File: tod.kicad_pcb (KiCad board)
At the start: 2 copper layers, 72 x 57 mm, 68 parts, among them J1 Conn_01x04, J2 Conn_01x03, J3 Conn_01x04, J4 Conn_01x03, Q1 BC856B, Q2 BC817, Q3 BC856B, Q4 BC817, Q5 BC856, Q6 BC817, Q7 BC856, Q8 BC817, U1 PC817, U2 PC817, U3 PC817, U4 PC817

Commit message: Use 2k resistors instead of 3k9.
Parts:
- R13, R18, R3, R8: value 3k9 -> 2k
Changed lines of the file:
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@@
     (descr "Resistor SMD 0805 (2012 Metric), square (rectangular) end terminal, IPC_7351 nominal with elongated pad for handsoldering. (Body size source: IPC-SM-782 page 72, https://www.pcb-3d.com/wordpress/wp-content/uploads/ipc-sm-782a_amendment_1_and_2.pdf), generated with kicad-footprint-generator")
     (tags "resistor handsolder")
-    (property "LCSC" "C17614")
+    (property "LCSC" "C17604")
     (property "Sheetfile" "tod.kicad_sch")
     (property "Sheetname" "")
@@
       (effects (font (size 1 1) (thickness 0.15)) (justify mirror))
     )
-    (fp_text value "3k9" (at 0 -1.65 90) (layer "B.Fab")
+    (fp_text value "2k" (at 0 -1.65 90) (layer "B.Fab")
       (effects (font (size 1 1) (thickness 0.15)) (justify mirror))
     )
@@
     (descr "SOD-323")
     (tags "SOD-323")
+    (property "JLCPCB_IGNORE" "-")
     (property "LCSC" "C191023")
     (property "Sheetfile" "tod.kicad_sch")
@@
     (descr "SOD-323")
     (tags "SOD-323")
+    (property "JLCPCB_IGNORE" "-")
     (property "LCSC" "C191023")
     (property "Sheetfile" "tod.kicad_sch")
@@
     (descr "Resistor SMD 0805 (2012 Metric), square (rectangular) end terminal, IPC_7351 nominal with elongated pad for handsoldering. (Body size source: IPC-SM-782 page 72, https://www.pcb-3d.com/wordpress/wp-content/uploads/ipc-sm-782a_amendment_1_and_2.pdf), generated with kicad-footprint-generator")
     (tags "resistor handsolder")
-    (property "LCSC" "C17614")
+    (property "LCSC" "C17604")
     (property "Sheetfile" "tod.kicad_sch")
     (property "Sheetname" "")
@@
       (effects (font (size 1 1) (thickness 0.15)) (justify mirror))
     )
-    (fp_text value "3k9" (at 0 -1.65 90) (layer "B.Fab")
+    (fp_text value "2k" (at 0 -1.65 90) (layer "B.Fab")
       (effects (font (size 1 1) (thickness 0.15)) (justify mirror))
     )
@@
     (descr "SOT, 3 Pin (https://www.jedec.org/system/files/docs/to-236h.pdf variant AB), generated with kicad-footprint-generator ipc_gullwing_generator.py")
     (tags "SOT TO_SOT_SMD")
-    (property "LCSC" "C2926215")
+    (property "LCSC" "C2149")
     (property "Sheetfile" "tod.kicad_sch")
     (property "Sheetname" "")
@@
     (descr "SOT, 3 Pin (https://www.jedec.org/system/files/docs/to-236h.pdf variant AB), generated with kicad-footprint-generator ipc_gullwing_generator.py")
     (tags "SOT TO_SOT_SMD")
-    (property "LCSC" "C2926215")
+    (property "LCSC" "C2149")
     (property "Sheetfile" "tod.kicad_sch")
     (property "Sheetname" "")
@@
     (descr "SOT, 3 Pin (https://www.jedec.org/system/files/docs/to-236h.pdf variant AB), generated with kicad-footprint-generator ipc_gullwing_generator.py")
     (tags "SOT TO_SOT_SMD")
-    (property "LCSC" "C2926215")
+    (property "LCSC" "C2149")
     (property "Sheetfile" "tod.kicad_sch")
     (property "Sheetname" "")
@@
     (descr "Resistor SMD 0805 (2012 Metric), square (rectangular) end terminal, IPC_7351 nominal with elongated pad for handsoldering. (Body size source: IPC-SM-782 page 72, https://www.pcb-3d.com/wordpress/wp-content/uploads/ipc-sm-782a_amendment_1_and_2.pdf), generated with kicad-footprint-generator")
     (tags "resistor handsolder")
-    (property "LCSC" "C17614")
+    (property "LCSC" "C17604")
     (property "Sheetfile" "tod.kicad_sch")
     (property "Sheetname" "")
@@
       (effects (font (size 1 1) (thickness 0.15)) (justify mirror))
     )
-    (fp_text value "3k9" (at 0 -1.65 90) (layer "B.Fab")
+    (fp_text value "2k" (at 0 -1.65 90) (layer "B.Fab")
       (effects (font (size 1 1) (thickness 0.15)) (justify mirror))
     )
@@
     (descr "Resistor SMD 0805 (2012 Metric), square (rectangular) end terminal, IPC_7351 nominal with elongated pad for handsoldering. (Body size source: IPC-SM-782 page 72, https://www.pcb-3d.com/wordpress/wp-content/uploads/ipc-sm-782a_amendment_1_and_2.pdf), generated with kicad-footprint-generator")
     (tags "resistor handsolder")
-    (property "LCSC" "C17614")
+    (property "LCSC" "C17604")
     (property "Sheetfile" "tod.kicad_sch")
     (property "Sheetname" "")
@@
       (effects (font (size 1 1) (thickness 0.15)) (justify mirror))
     )
-    (fp_text value "3k9" (at 0 -1.65 90) (layer "B.Fab")
+    (fp_text value "2k" (at 0 -1.65 90) (layer "B.Fab")
       (effects (font (size 1 1) (thickness 0.15)) (justify mirror))
     )
@@
     (descr "SOD-323")
     (tags "SOD-323")
+    (property "JLCPCB_IGNORE" "-")
     (property "LCSC" "C191023")
     (property "Sheetfile" "tod.kicad_sch")
@@
     (descr "SOT, 3 Pin (https://www.jedec.org/system/files/docs/to-236h.pdf variant AB), generated with kicad-footprint-generator ipc_gullwing_generator.py")
     (tags "SOT TO_SOT_SMD")
-    (property "LCSC" "C2926215")
+    (property "LCSC" "C2149")
     (property "Sheetfile" "tod.kicad_sch")
     (property "Sheetname" "")
@@
     (descr "SOD-323")
     (tags "SOD-323")
+    (property "JLCPCB_IGNORE" "-")
     (property "LCSC" "C191023")
     (property "Sheetfile" "tod.kicad_sch")

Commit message: Revert "Use 2k resistors instead of 3k9."
This reverts commit e4b48c20f046feec0504172c1823d5e465362b53.
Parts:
- R13, R18, R3, R8: value 2k -> 3k9
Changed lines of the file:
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@@
     (descr "Resistor SMD 0805 (2012 Metric), square (rectangular) end terminal, IPC_7351 nominal with elongated pad for handsoldering. (Body size source: IPC-SM-782 page 72, https://www.pcb-3d.com/wordpress/wp-content/uploads/ipc-sm-782a_amendment_1_and_2.pdf), generated with kicad-footprint-generator")
     (tags "resistor handsolder")
-    (property "LCSC" "C17604")
+    (property "LCSC" "C17614")
     (property "Sheetfile" "tod.kicad_sch")
     (property "Sheetname" "")
@@
       (effects (font (size 1 1) (thickness 0.15)) (justify mirror))
     )
-    (fp_text value "2k" (at 0 -1.65 90) (layer "B.Fab")
+    (fp_text value "3k9" (at 0 -1.65 90) (layer "B.Fab")
       (effects (font (size 1 1) (thickness 0.15)) (justify mirror))
     )
@@
     (descr "SOD-323")
     (tags "SOD-323")
-    (property "JLCPCB_IGNORE" "-")
     (property "LCSC" "C191023")
     (property "Sheetfile" "tod.kicad_sch")
@@
     (descr "SOD-323")
     (tags "SOD-323")
-    (property "JLCPCB_IGNORE" "-")
     (property "LCSC" "C191023")
     (property "Sheetfile" "tod.kicad_sch")
@@
     (descr "Resistor SMD 0805 (2012 Metric), square (rectangular) end terminal, IPC_7351 nominal with elongated pad for handsoldering. (Body size source: IPC-SM-782 page 72, https://www.pcb-3d.com/wordpress/wp-content/uploads/ipc-sm-782a_amendment_1_and_2.pdf), generated with kicad-footprint-generator")
     (tags "resistor handsolder")
-    (property "LCSC" "C17604")
+    (property "LCSC" "C17614")
     (property "Sheetfile" "tod.kicad_sch")
     (property "Sheetname" "")
@@
       (effects (font (size 1 1) (thickness 0.15)) (justify mirror))
     )
-    (fp_text value "2k" (at 0 -1.65 90) (layer "B.Fab")
+    (fp_text value "3k9" (at 0 -1.65 90) (layer "B.Fab")
       (effects (font (size 1 1) (thickness 0.15)) (justify mirror))
     )
@@
     (descr "SOT, 3 Pin (https://www.jedec.org/system/files/docs/to-236h.pdf variant AB), generated with kicad-footprint-generator ipc_gullwing_generator.py")
     (tags "SOT TO_SOT_SMD")
-    (property "LCSC" "C2149")
+    (property "LCSC" "C2926215")
     (property "Sheetfile" "tod.kicad_sch")
     (property "Sheetname" "")
@@
     (descr "SOT, 3 Pin (https://www.jedec.org/system/files/docs/to-236h.pdf variant AB), generated with kicad-footprint-generator ipc_gullwing_generator.py")
     (tags "SOT TO_SOT_SMD")
-    (property "LCSC" "C2149")
+    (property "LCSC" "C2926215")
     (property "Sheetfile" "tod.kicad_sch")
     (property "Sheetname" "")
@@
     (descr "SOT, 3 Pin (https://www.jedec.org/system/files/docs/to-236h.pdf variant AB), generated with kicad-footprint-generator ipc_gullwing_generator.py")
     (tags "SOT TO_SOT_SMD")
-    (property "LCSC" "C2149")
+    (property "LCSC" "C2926215")
     (property "Sheetfile" "tod.kicad_sch")
     (property "Sheetname" "")
@@
     (descr "Resistor SMD 0805 (2012 Metric), square (rectangular) end terminal, IPC_7351 nominal with elongated pad for handsoldering. (Body size source: IPC-SM-782 page 72, https://www.pcb-3d.com/wordpress/wp-content/uploads/ipc-sm-782a_amendment_1_and_2.pdf), generated with kicad-footprint-generator")
     (tags "resistor handsolder")
-    (property "LCSC" "C17604")
+    (property "LCSC" "C17614")
     (property "Sheetfile" "tod.kicad_sch")
     (property "Sheetname" "")
@@
       (effects (font (size 1 1) (thickness 0.15)) (justify mirror))
     )
-    (fp_text value "2k" (at 0 -1.65 90) (layer "B.Fab")
+    (fp_text value "3k9" (at 0 -1.65 90) (layer "B.Fab")
       (effects (font (size 1 1) (thickness 0.15)) (justify mirror))
     )
@@
     (descr "Resistor SMD 0805 (2012 Metric), square (rectangular) end terminal, IPC_7351 nominal with elongated pad for handsoldering. (Body size source: IPC-SM-782 page 72, https://www.pcb-3d.com/wordpress/wp-content/uploads/ipc-sm-782a_amendment_1_and_2.pdf), generated with kicad-footprint-generator")
     (tags "resistor handsolder")
-    (property "LCSC" "C17604")
+    (property "LCSC" "C17614")
     (property "Sheetfile" "tod.kicad_sch")
     (property "Sheetname" "")
@@
       (effects (font (size 1 1) (thickness 0.15)) (justify mirror))
     )
-    (fp_text value "2k" (at 0 -1.65 90) (layer "B.Fab")
+    (fp_text value "3k9" (at 0 -1.65 90) (layer "B.Fab")
       (effects (font (size 1 1) (thickness 0.15)) (justify mirror))
     )
@@
     (descr "SOD-323")
     (tags "SOD-323")
-    (property "JLCPCB_IGNORE" "-")
     (property "LCSC" "C191023")
     (property "Sheetfile" "tod.kicad_sch")
@@
     (descr "SOT, 3 Pin (https://www.jedec.org/system/files/docs/to-236h.pdf variant AB), generated with kicad-footprint-generator ipc_gullwing_generator.py")
     (tags "SOT TO_SOT_SMD")
-    (property "LCSC" "C2149")
+    (property "LCSC" "C2926215")
     (property "Sheetfile" "tod.kicad_sch")
     (property "Sheetname" "")
@@
     (descr "SOD-323")
     (tags "SOD-323")
-    (property "JLCPCB_IGNORE" "-")
     (property "LCSC" "C191023")
     (property "Sheetfile" "tod.kicad_sch")

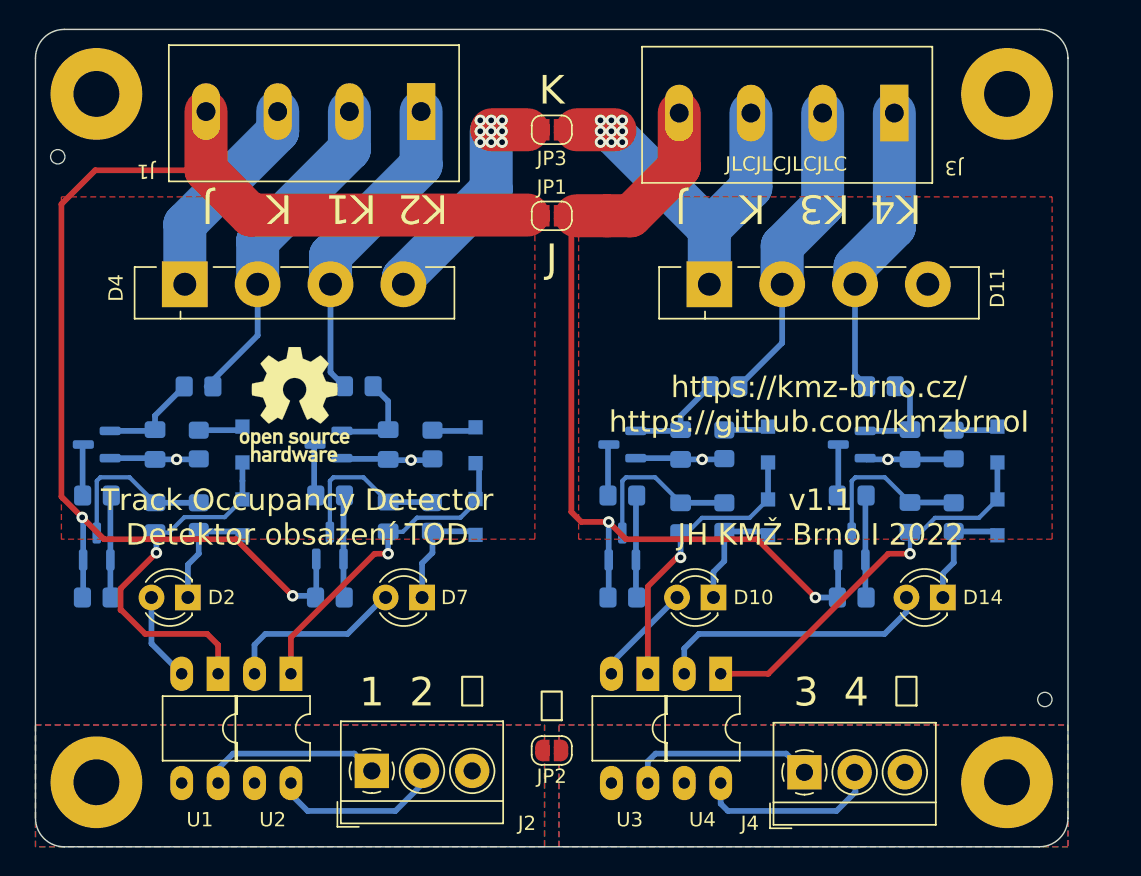
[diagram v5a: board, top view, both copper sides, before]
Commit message: Add capacitor value to silkscreen.
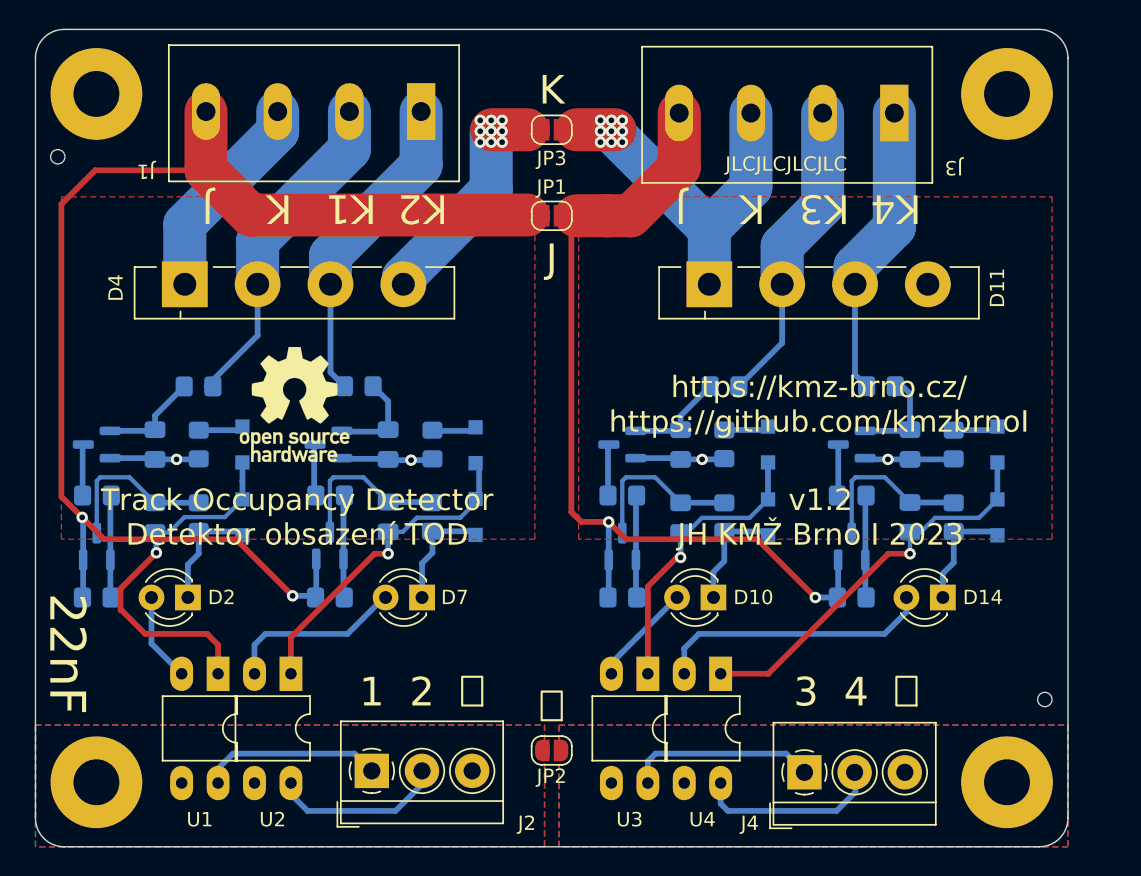
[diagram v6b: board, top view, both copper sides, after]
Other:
- board text added: "22nF"
- board text added: "v1.2 JH KMŽ Brno I 2023"
- board text removed: "v1.1 JH KMŽ Brno I 2022"
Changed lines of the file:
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@@
     (effects (font (size 2 2) (thickness 0.15)))
   )
-  (gr_text "v1.1\nJH KMŽ Brno I 2022" (at 167.75 97.028) (layer "F.SilkS")
+  (gr_text "v1.2\nJH KMŽ Brno I 2023" (at 167.75 97.028) (layer "F.SilkS")
     (effects (font (size 1.5 1.5) (thickness 0.15)))
   )
@@
     (effects (font (size 2 2) (thickness 0.15)))
   )
+  (gr_text "22nF" (at 115.189 106.553 270) (layer "F.SilkS")
+    (effects (font (size 2.5 2.5) (thickness 0.3)))
+  )
   (gr_text "1" (at 136.454 109.22) (layer "F.SilkS")

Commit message: Use electrolytic capacitors for 22uF C.
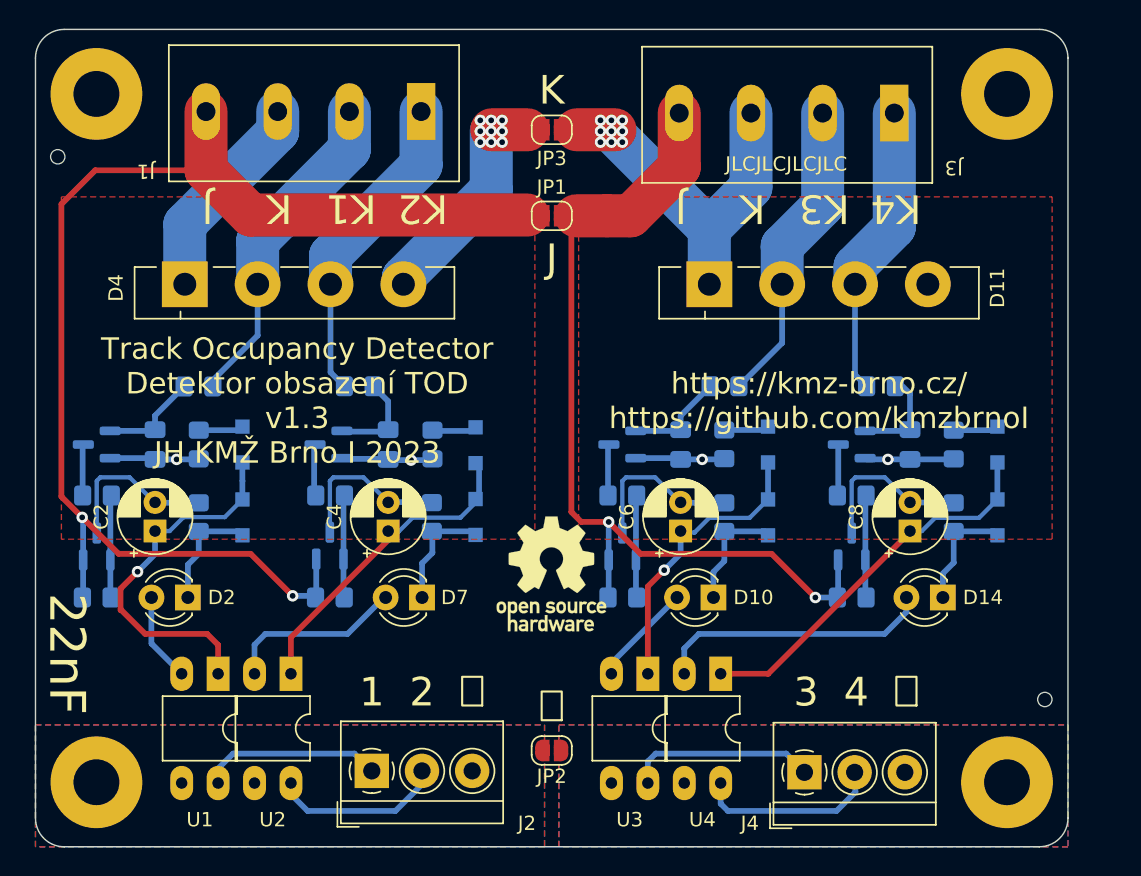
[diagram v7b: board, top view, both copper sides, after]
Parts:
- C2, C4, C6, C8: footprint Capacitor_SMD:C_0805_2012Metric_Pad1.18x1.45mm_HandSolder -> Capacitor_THT:CP_Radial_D5.0mm_P2.00mm; moved to F.Cu
- J1, J3: value Conn_01x04 -> 2xMVE252
- J2, J4: value Conn_01x03 -> MV133
- moved REF** 21.5 mm to (149.0, 101.0)
- moved C4 0.98 mm to (137.6, 98.0)
- moved C8 0.96 mm to (174.0, 98.0)
- moved C2 0.93 mm to (121.3, 98.0)
- moved C6 0.93 mm to (158.0, 98.0)
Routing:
- net Net-(C8-Pad1): track 27.8 -> 27.0 mm, vias 1 -> 0
- net Net-(C4-Pad1): track 23.2 -> 22.7 mm, vias 1 -> 0
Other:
- board text added: "Track Occupancy Detector Detektor obsazení TOD v1.3 JH KMŽ Brno I 2023"
- board text removed: "Track Occupancy Detector Detektor obsazení TOD"
- board text removed: "v1.2 JH KMŽ Brno I 2023"
